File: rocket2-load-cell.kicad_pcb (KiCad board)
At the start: 4 copper layers, 0 parts

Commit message: added working arduino code as well as testread.py(nonop)
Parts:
- added ADS1219: ~, Package_SO:TSSOP-16_4.4x5mm_P0.65mm, F.Cu at (97.0, 56.5)
- added C1: 0.1uF, Capacitor_SMD:C_0603_1608Metric, F.Cu at (115.4, 94.8)
- added C10: 100nF, Capacitor_SMD:C_0603_1608Metric, F.Cu at (119.4, 99.8)
- added C11: 22uF, Capacitor_SMD:C_0603_1608Metric, F.Cu at (119.4, 102.4)
- added C12: 10uF, Capacitor_SMD:C_0603_1608Metric, F.Cu at (119.4, 104.9)
- added C13: 100nF, Capacitor_SMD:C_0603_1608Metric, F.Cu at (119.4, 107.4)
- added C14: 100nF, Capacitor_SMD:C_0603_1608Metric, F.Cu at (88.5, 66.8)
- added C15: 100nF, Capacitor_SMD:C_0603_1608Metric, F.Cu at (123.4, 97.3)
- added C16: 0.1uF, Capacitor_SMD:C_0603_1608Metric_Pad1.08x0.95mm_HandSolder, F.Cu at (143.8, 101.4)
- added C18: 10uF, Capacitor_SMD:C_0603_1608Metric, F.Cu at (123.4, 99.8)
- added C19: 0.1uF, Capacitor_SMD:C_0603_1608Metric_Pad1.08x0.95mm_HandSolder, F.Cu at (143.8, 103.9)
- added C2: 100nF, Capacitor_SMD:C_0603_1608Metric, F.Cu at (88.0, 82.0)
- added C20: 0.1uF, Capacitor_SMD:C_0603_1608Metric, F.Cu at (101.5, 55.0)
- added C3: 100nF, Capacitor_SMD:C_0603_1608Metric, F.Cu at (97.5, 76.0)
- added C5: 100nF, Capacitor_SMD:C_0603_1608Metric, F.Cu at (88.5, 70.0)
- added C6: 100nF, Capacitor_SMD:C_0603_1608Metric, F.Cu at (101.0, 67.8)
- added C7: 100nF, Capacitor_SMD:C_0603_1608Metric, F.Cu at (92.2, 64.0)
- added C8: 100nF, Capacitor_SMD:C_0603_1608Metric, F.Cu at (88.5, 73.3)
- added C9: 22uF, Capacitor_SMD:C_0603_1608Metric, F.Cu at (119.4, 97.3)
- added D1: GREEN_LED, LED_SMD:LED_0603_1608Metric, F.Cu at (90.7, 62.0)
- added J1: SWD, Connector_PinHeader_1.27mm:PinHeader_2x05_P1.27mm_Vertical_SMD, F.Cu at (105.5, 64.5)
- added J2: Screw_Terminal_01x02, TerminalBlock_Phoenix:TerminalBlock_Phoenix_MKDS-1,5-2-5.08_1x02_P5.08mm_Horizontal, F.Cu at (115.5, 82.6)
- added JP1: M05PTH, TerminalBlock_Phoenix:TerminalBlock_Phoenix_MKDS-1,5-5-5.08_1x05_P5.08mm_Horizontal, F.Cu at (115.5, 68.5)
- added L2: 3.3uH, Inductor_SMD:L_0603_1608Metric, F.Cu at (123.4, 104.9)
- added R1: 10k, Resistor_SMD:R_0603_1608Metric, F.Cu at (123.4, 107.4)
- added R2: 100, Resistor_SMD:R_0603_1608Metric, F.Cu at (104.0, 56.5)
- added R3: 10k, Resistor_SMD:R_0603_1608Metric, F.Cu at (127.4, 97.3)
- added R4: 100, Resistor_SMD:R_0603_1608Metric, F.Cu at (104.0, 53.5)
- added R5: 470, Resistor_SMD:R_0603_1608Metric, F.Cu at (89.0, 64.0)
- added U1: ~, Package_SO:SOIC-8W_5.3x5.3mm_P1.27mm, F.Cu at (92.9, 81.8)
- added U2: STM32F103C8Tx, Package_QFP:LQFP-48_7x7mm_P0.5mm, F.Cu at (94.8, 70.0)
- added U3: AMS1117-3.3, Package_TO_SOT_SMD:SOT-223-3_TabPin2, F.Cu at (105.5, 81.0)
- added Y1: 16MHz, Crystal:Crystal_SMD_2520-4Pin_2.5x2.0mm, F.Cu at (84.8, 70.2)
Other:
- copper layers 4 -> 2

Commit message: fixed back up issue
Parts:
- removed C10, C15: 100nF, Capacitor_SMD:C_0603_1608Metric
- removed C12: 10uF, Capacitor_SMD:C_0603_1608Metric
- added H1: MountingHole, MountingHole:MountingHole_3.2mm_M3, F.Cu at (169.5, 85.5)
- added H2: MountingHole, MountingHole:MountingHole_3.2mm_M3, F.Cu at (135.5, 85.5)
- added H3: MountingHole, MountingHole:MountingHole_3.2mm_M3, F.Cu at (135.5, 131.0)
- added H4: MountingHole, MountingHole:MountingHole_3.2mm_M3, F.Cu at (169.5, 131.0)
- moved J1 69.4 mm to (157.2, 110.8), turned to 0 degrees
- moved R4 68.9 mm to (160.5, 93.0)
- moved C20 68.7 mm to (158.0, 94.0), turned to 90 degrees
- moved JP1 68.6 mm to (168.0, 112.7)
- moved R2 68.4 mm to (160.5, 95.0)
- moved ADS1219 68.0 mm to (153.0, 95.0), turned to 180 degrees
- moved J2 66.9 mm to (168.0, 124.1)
- moved U3 65.5 mm to (158.5, 119.5)
- moved U1 65.3 mm to (147.0, 118.5)
- moved C5 64.7 mm to (141.2, 107.5)
- moved C8 64.5 mm to (141.2, 110.5), turned to 90 degrees
- moved Y1 64.4 mm to (138.0, 106.5), turned to 0 degrees
- moved C14 64.4 mm to (141.2, 103.8)
- moved C3 64.4 mm to (150.2, 113.0)
- moved C7 64.4 mm to (144.9, 101.0)
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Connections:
- ADS1219 pad 3: ADS_RESET -> Net-(ADS1219-RESET)
- C14 pad 1: GND -> +3.3V
- C14 pad 2: +3.3V -> GND
- JP1 pad 2: AIN+ -> GND
- JP1 pad 3: AIN- -> Net-(C13-Pad1)
- JP1 pad 4: GND -> AIN-
- JP1 pad 5: Net-(C13-Pad1) -> AIN+
- R3 pad 1: ADS_RESET -> Net-(ADS1219-RESET)
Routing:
- net +3.3V: track 0.00 -> 146.4 mm, vias 0 -> 2
- net GND: track 0.00 -> 39.7 mm, vias 0 -> 11
- net VBUS: track 0.00 -> 25.8 mm
- net NRST: track 0.00 -> 19.4 mm
- net MEM_WP: track 0.00 -> 18.1 mm, vias 0 -> 2
- net Net-(C13-Pad1): track 0.00 -> 16.7 mm
- net MEM_MISO: track 0.00 -> 14.5 mm, vias 0 -> 2
- net MEM_CS: track 0.00 -> 14.5 mm, vias 0 -> 2
- net DEBUG_SWDIO: track 0.00 -> 12.5 mm
- net ADS_DRDY: track 0.00 -> 12.0 mm
- net DEBUG_SWCLK: track 0.00 -> 9.96 mm
- net ADS_DATA: track 0.00 -> 7.84 mm
- net AIN-: track 0.00 -> 7.68 mm
- net ADS_CLK: track 0.00 -> 6.95 mm
- net AIN+: track 0.00 -> 6.95 mm
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- added copper zone on B.Cu, net GND
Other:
- board outline added: 42 x 53.5 mm

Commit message: added images and made it coooooooooooooollllllllllllllllllllllllllllllllllllllllllllllllllll
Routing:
- net +3.3V: track 146.4 -> 165.8 mm, vias 2 -> 4
- net GND: track 39.7 -> 56.5 mm, vias 11 -> 17
- net NRST: track 19.4 -> 21.7 mm

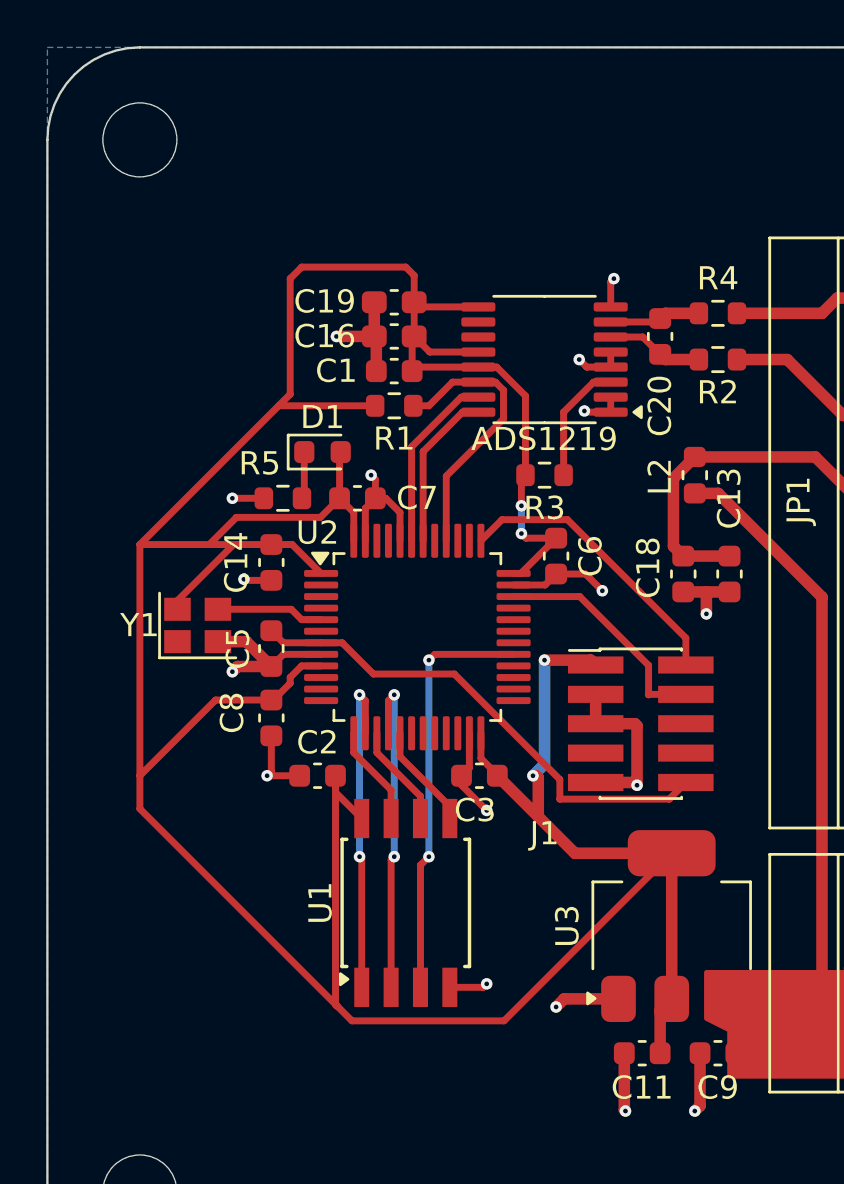
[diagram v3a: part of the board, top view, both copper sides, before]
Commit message: added cool images to loadcell silk screen
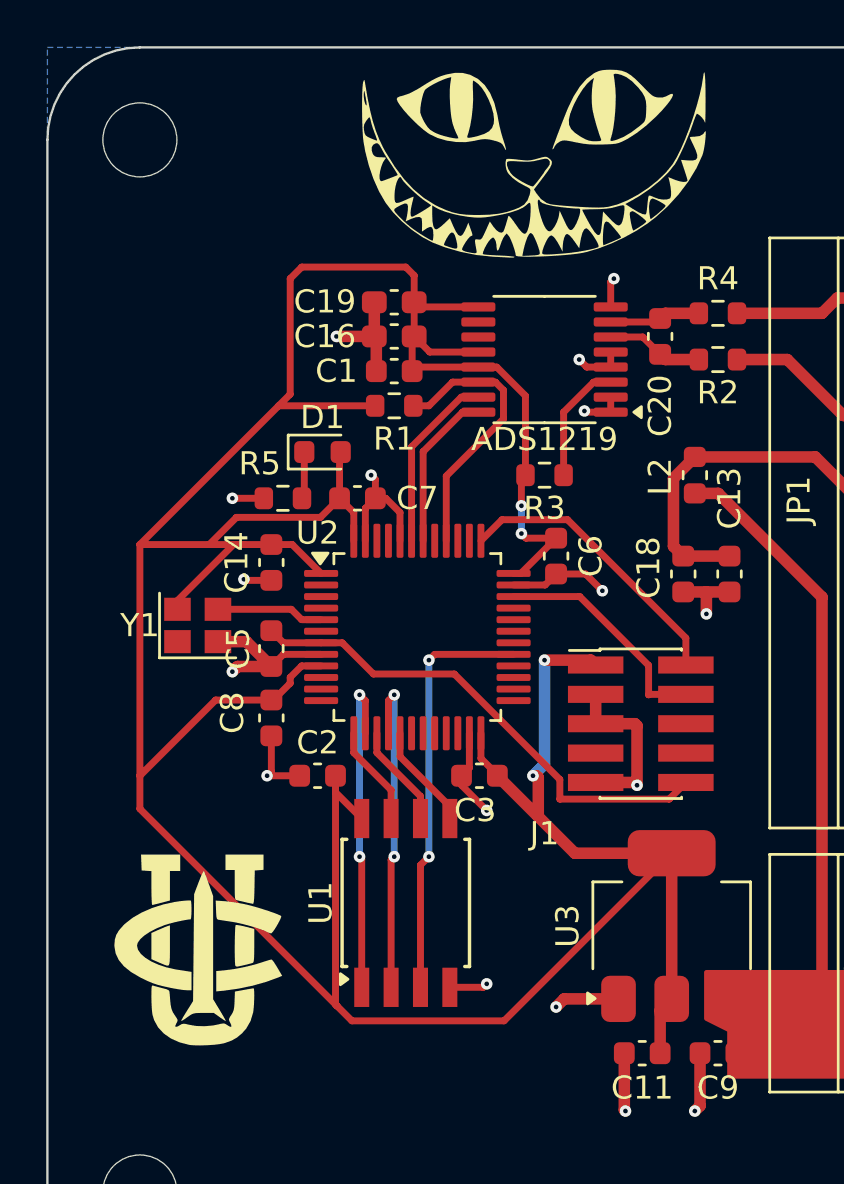
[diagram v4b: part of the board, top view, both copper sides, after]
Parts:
- added G***: LOGO, UCILIB:uci_rocket_logo, F.Cu at (138.0, 120.5)
- added G***: LOGO, UCILIB:cat_logo, F.Cu at (152.5, 86.5)

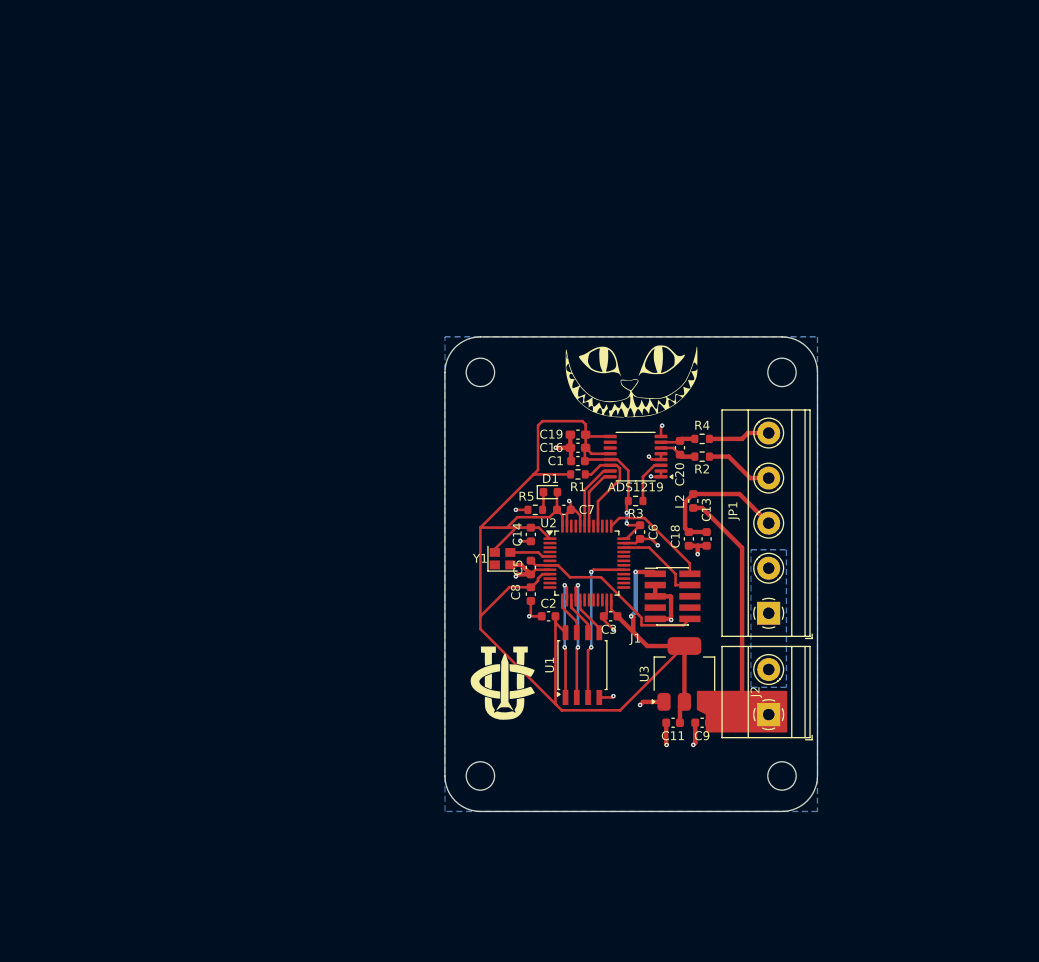
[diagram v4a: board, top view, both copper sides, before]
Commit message: added ethernet module as well as fixing some wireing issues
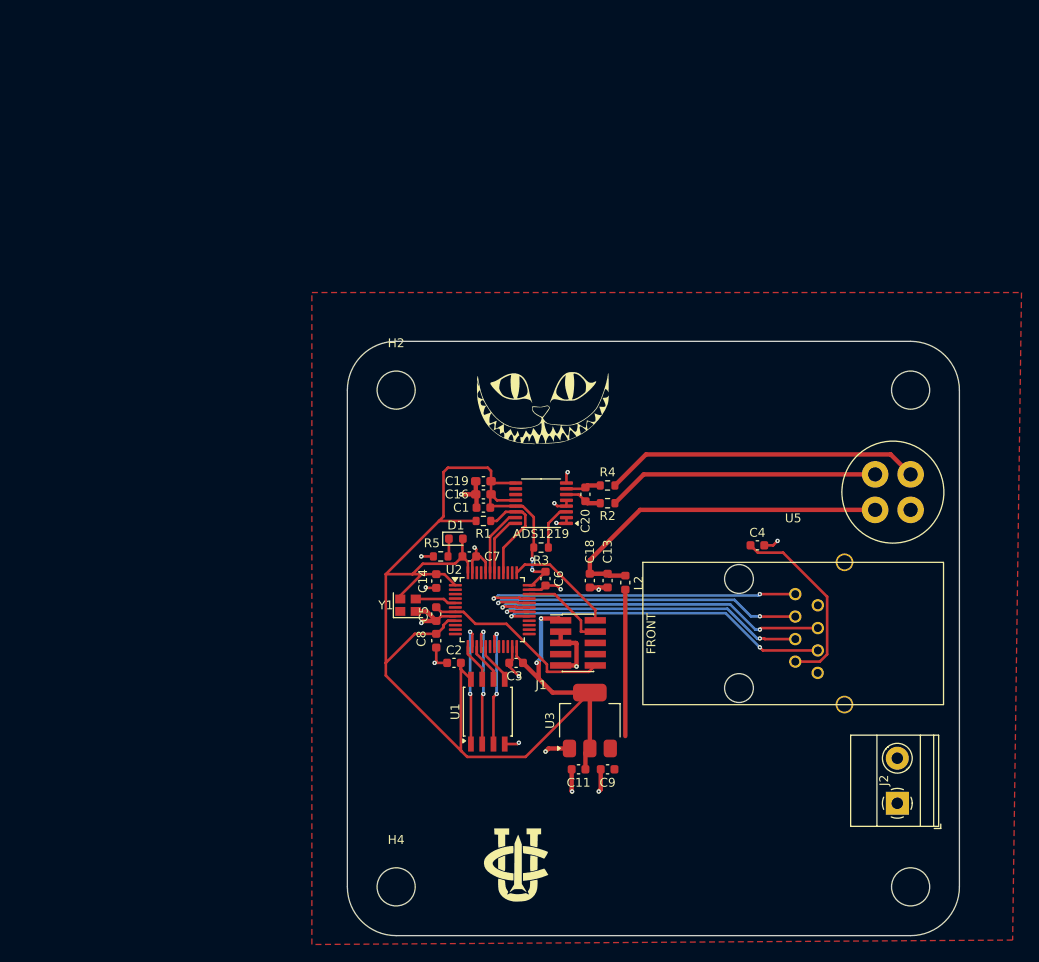
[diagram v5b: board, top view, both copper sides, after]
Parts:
- removed JP1: M05PTH, TerminalBlock_Phoenix:TerminalBlock_Phoenix_MKDS-1,5-5-5.08_1x05_P5.08mm_Horizontal
- added C4: 4.7uF, Capacitor_SMD:C_0603_1608Metric, F.Cu at (166.7, 105.0)
- added GX12: ~, UCIRP-KiCAD-Lib:gx12, F.Cu at (182.0, 99.0)
- added U5: ~, GSE:GC-XPORT, F.Cu at (170.8, 114.9)
- H1, H2, H3, H4: footprint MountingHole:MountingHole_3.2mm_M3 -> MountingHole:MountingHole_4.3mm_M4
- moved H3 65.1 mm to (184.0, 87.5)
- moved H1 59.8 mm to (184.0, 143.5)
- moved H4 45.3 mm to (126.0, 143.5)
- moved G*** 20.6 mm to (139.5, 141.0)
- moved J2 17.6 mm to (182.5, 134.1)
- moved C13 12.1 mm to (149.8, 109.0)
- moved C18 12.1 mm to (147.8, 109.0)
- moved L2 12.0 mm to (151.8, 109.2)
- moved ADS1219 11.9 mm to (142.3, 100.2)
- moved C1 11.9 mm to (135.8, 100.8)
- moved C11 11.9 mm to (146.6, 130.2)
- moved C14 11.9 mm to (130.5, 109.0)
- moved C16 11.9 mm to (135.8, 99.2)
- moved C19 11.9 mm to (135.8, 97.8)
- moved C2 11.9 mm to (132.5, 118.2)
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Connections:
- U2 pad 19: unconnected-(U2-PB1-Pad19) -> MEM_WP
- U2 pad 29: MEM_WP -> ETH_~{RST}
- U2 pad 30: unconnected-(U2-PA9-Pad30) -> ETH_TX
- U2 pad 31: unconnected-(U2-PA10-Pad31) -> ETH_RX
- U2 pad 32: unconnected-(U2-PA11-Pad32) -> ETH_RTS
- U2 pad 33: unconnected-(U2-PA12-Pad33) -> ETH_CTS
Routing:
- net ETH_RX: track 0.00 -> 40.0 mm, vias 0 -> 2
- net ETH_~{RST}: track 0.00 -> 38.4 mm, vias 0 -> 2
- net ETH_CTS: track 0.00 -> 38.3 mm, vias 0 -> 2
- net ETH_RTS: track 0.00 -> 38.0 mm, vias 0 -> 2
- net ETH_TX: track 0.00 -> 36.6 mm, vias 0 -> 2
- net AIN+: track 6.95 -> 35.7 mm
- net Net-(C13-Pad1): track 16.7 -> 40.1 mm
- net AIN-: track 7.68 -> 30.7 mm
- net +3.3V: track 165.8 -> 187.3 mm
- net VBUS: track 25.8 -> 16.5 mm
- net MEM_WP: track 18.1 -> 14.1 mm
- net GND: track 56.5 -> 57.1 mm, vias 17 -> 18
- added copper zone on F.Cu, net GND
- removed copper zone on B.Cu, net GND
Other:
- board size 42 x 53.5 mm -> 69 x 67 mm

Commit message: made it so that all vias are connected, should be good for fabrication, no design errors now
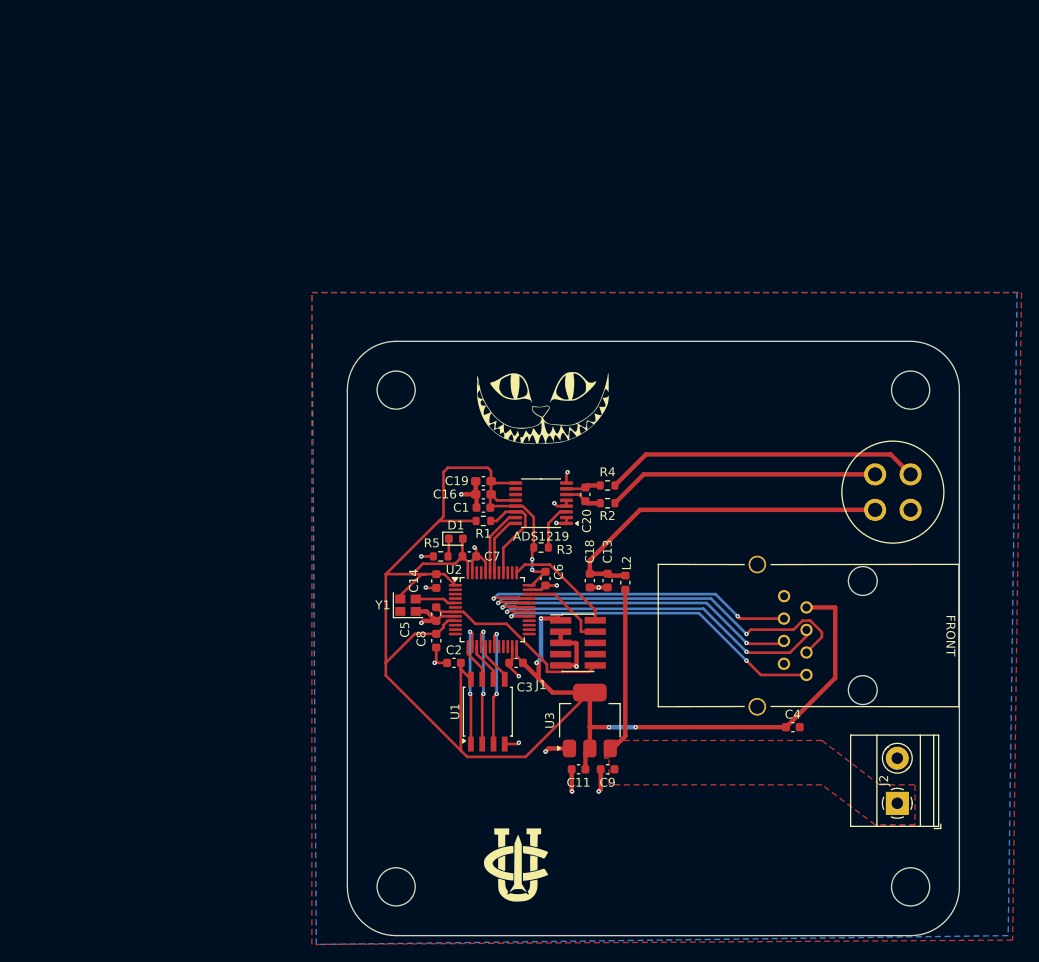
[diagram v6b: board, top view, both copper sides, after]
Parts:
- moved C4 20.9 mm to (170.7, 125.5)
- moved U5 1.76 mm to (172.5, 115.2), turned to 180 degrees
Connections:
- U2 pad 29: ETH_~{RST} -> ETH_CTS
- U2 pad 33: ETH_CTS -> ETH_~{RST}
- U2 pad 41: ADS_RESET -> unconnected-(U2-PB5-Pad41)
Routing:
- net +3.3V: track 187.3 -> 207.0 mm, vias 4 -> 6
- net ETH_RTS: track 38.0 -> 46.1 mm
- net ETH_TX: track 36.6 -> 40.0 mm
- net ETH_RX: track 40.0 -> 37.0 mm
- net GND: track 57.1 -> 54.6 mm, vias 18 -> 17
- net VBUS: track 16.5 -> 18.8 mm
- added copper zone on B.Cu, net GND
- added copper zone on F.Cu, net VBUS
